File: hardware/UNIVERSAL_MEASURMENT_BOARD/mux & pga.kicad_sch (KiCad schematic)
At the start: 12 parts, among them Q1 NMOS, U1 PGA280AIPW, U2 CD4067BM96, U3 CD4067BM96

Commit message: continued
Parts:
- renumbered C8 to C10, C7 to C11, C9 to C12, C10 to C13, C6 to C7, C12 to C8, C11 to C9, U2 to U3, U1 to U4, U3 to U5
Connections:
- net +15V renamed +15VA
- net +3.3V renamed +3.3VA
- net -15V renamed -15VA
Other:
- company: (none) -> PUT Motorsport Formula Student team
- title: (none) -> Universal Measurment Board
- moved on the sheet: C10, C11, C12, C13, C7, C8, C9, Q1, R1, U3, U4, U5

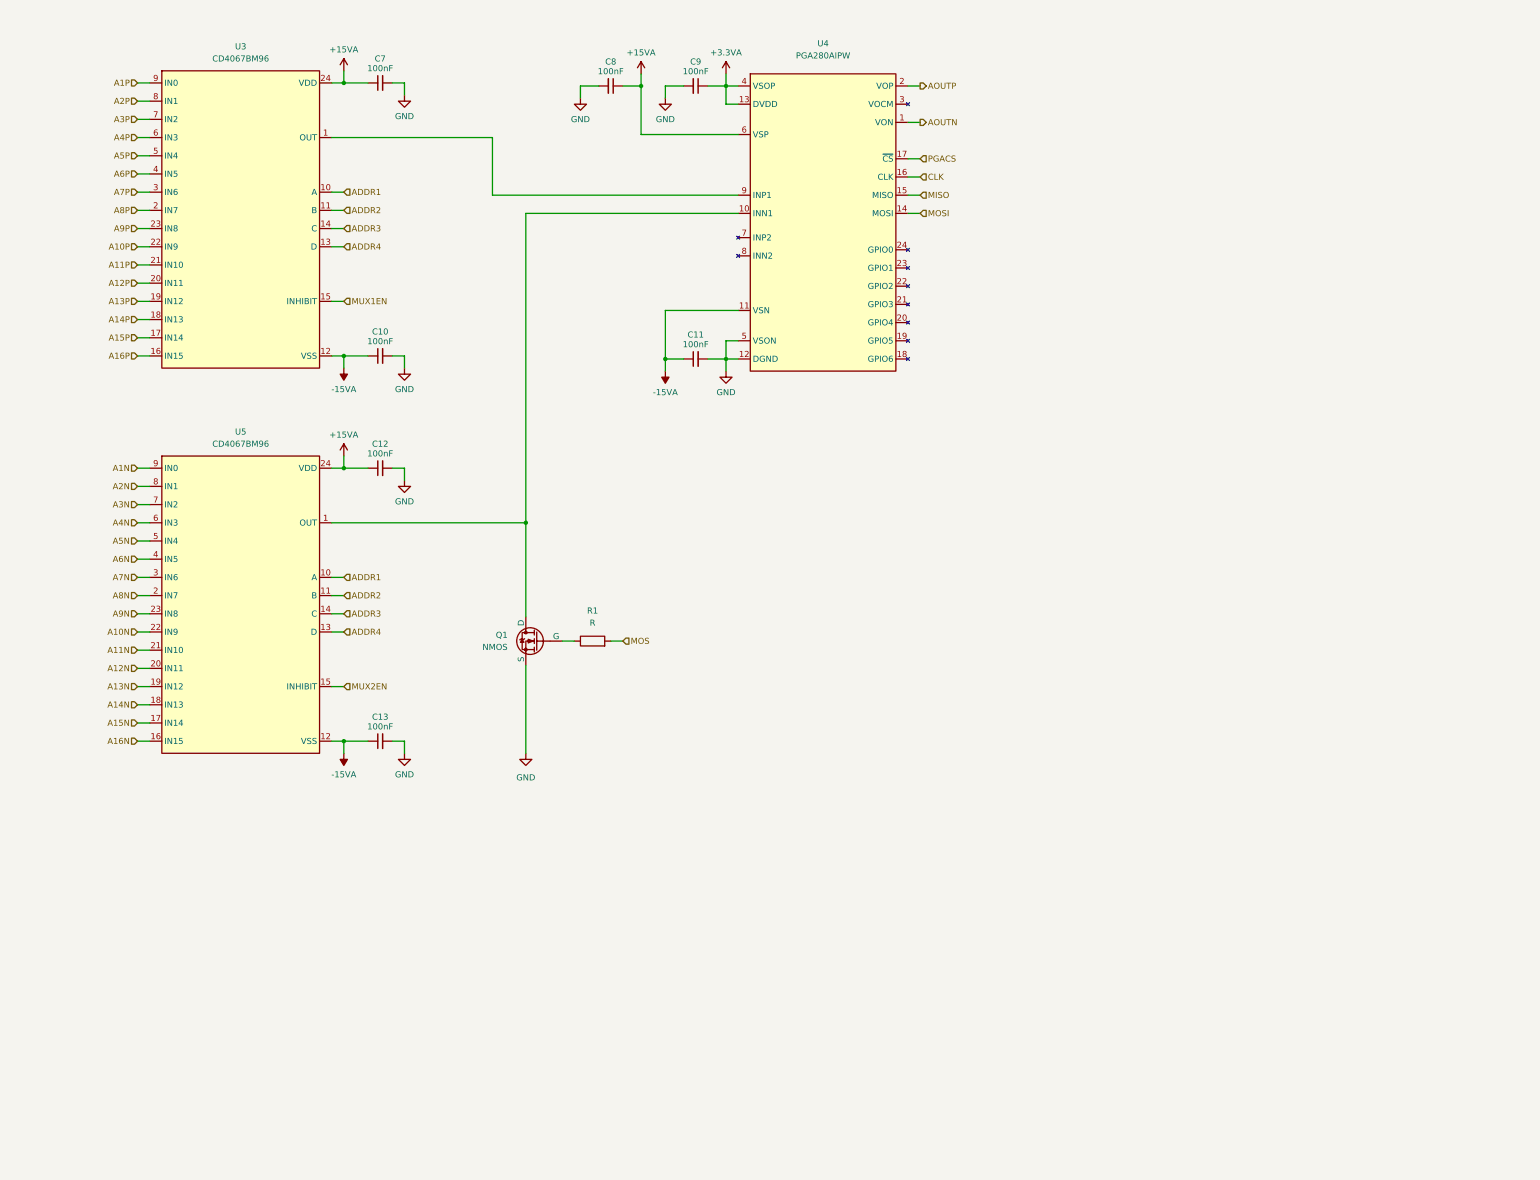
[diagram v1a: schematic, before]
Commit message: schematic review corrections
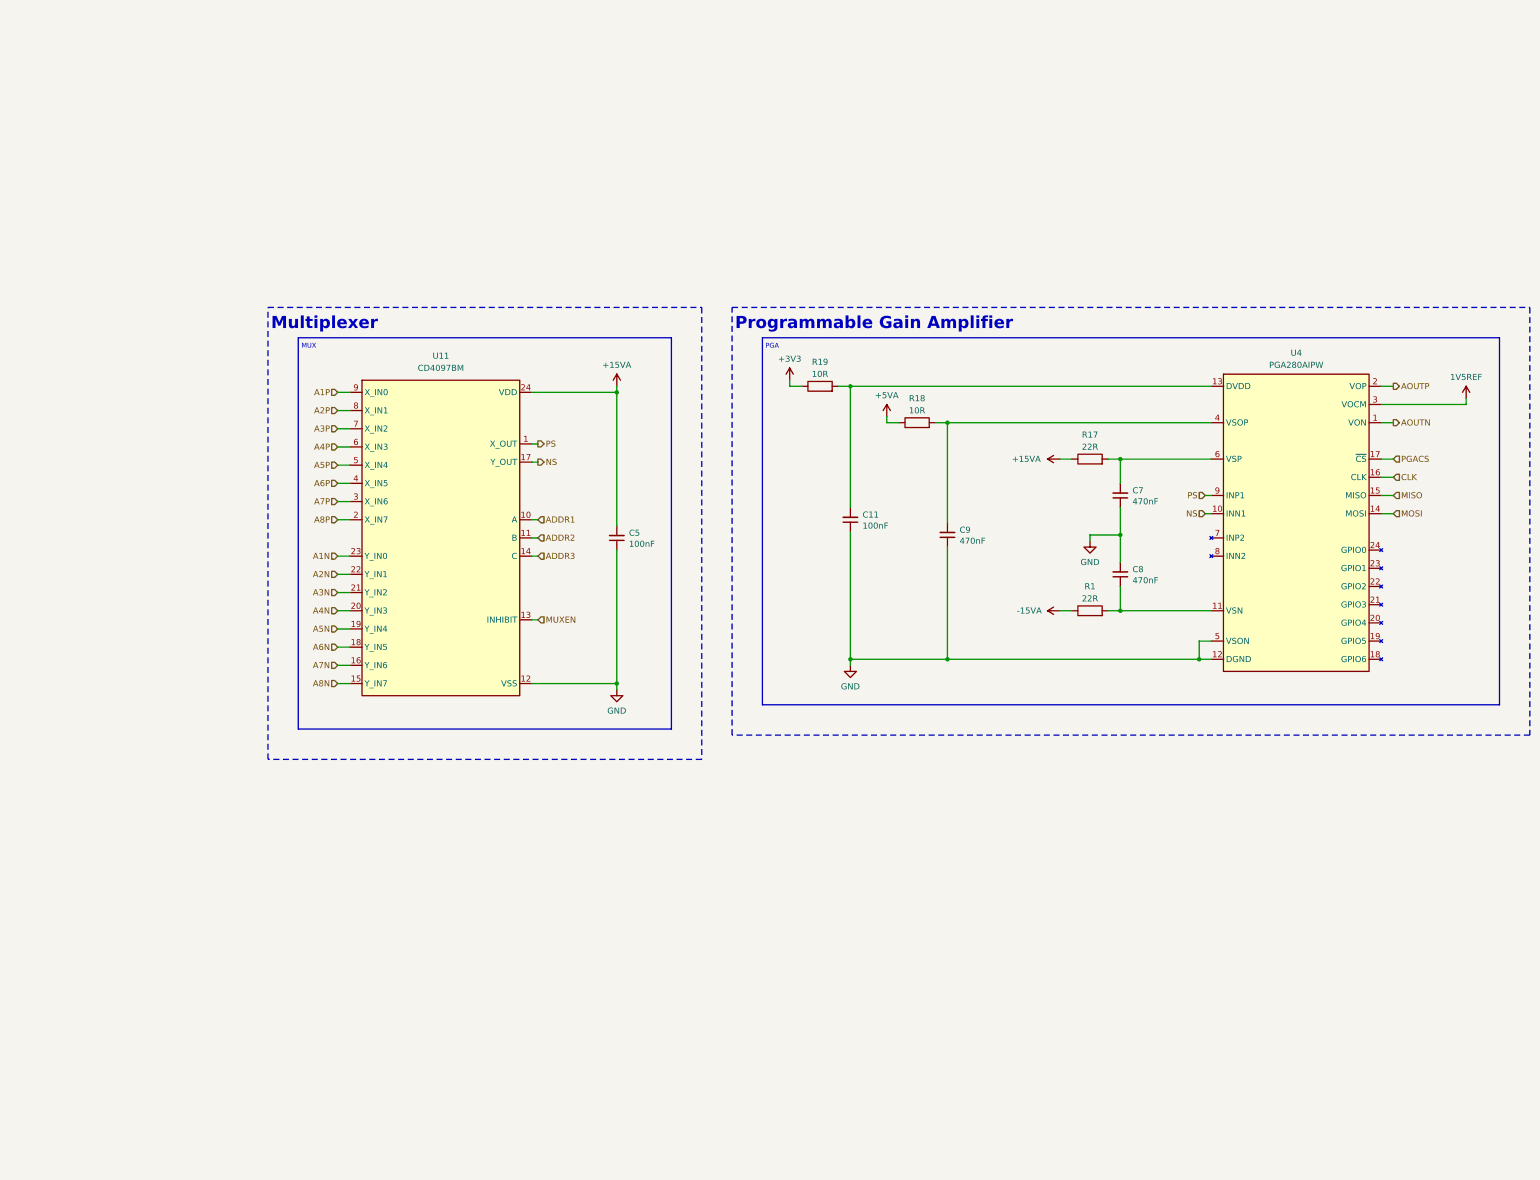
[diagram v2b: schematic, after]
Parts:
- removed C10, C12, C13: 100nF, symbol Device:C_Small
- removed Q1: NMOS, symbol Simulation_SPICE:NMOS
- removed U3, U5: CD4067BM96, SOIC127P1030X265-24N, symbol CD4067BM96:CD4067BM96
- added C5: 100nF, Capacitor_SMD:C_0805_2012Metric, symbol Device:C_Small
- added R17: 22R, symbol Device:R
- added R18, R19: 10R, symbol Device:R
- added U11: CD4097BM, SOIC127P1030X265-24N, symbol CD4097BM:CD4097BM
- C11: footprint (none) -> Capacitor_SMD:C_0805_2012Metric; Manufacturer_Name (none) -> MCASH21GCC7684MTCA1J; Manufacturer_Part_Number (none) -> CL21A107MQYNNWE; Mouser Part Number (none) -> 810-C2012X5R1V226MAC
- C7, C8, C9: value 100nF -> 470nF; footprint (none) -> Capacitor_SMD:C_0805_2012Metric; Manufacturer_Name (none) -> MCASH21GCC7684MTCA1J; Manufacturer_Part_Number (none) -> CL21A107MQYNNWE; Mouser Part Number (none) -> 810-C2012X5R1V226MAC
- R1: value R -> 22R
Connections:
- net +15VA: now also C5.2, R17.1, U11.24 (VDD); no longer C7.1, C8.1, U4.6 (VSP)
- net -15VA: now also R1.1; no longer C11.1, U4.11 (VSN)
- net A1N: now also U11.23 (Y_IN0)
- net A1P: now also U11.9 (X_IN0)
- net A2N: now also U11.22 (Y_IN1)
- net A2P: now also U11.8 (X_IN1)
- net A3N: now also U11.21 (Y_IN2)
- net A3P: now also U11.7 (X_IN2)
- net A4N: now also U11.20 (Y_IN3)
- net A4P: now also U11.6 (X_IN3)
- net A5N: now also U11.19 (Y_IN4)
- net A5P: now also U11.5 (X_IN4)
- net A6N: now also U11.18 (Y_IN5)
- net A6P: now also U11.4 (X_IN5)
- net A7N: now also U11.16 (Y_IN6)
- net A7P: now also U11.3 (X_IN6)
- net A8N: now also U11.15 (Y_IN7)
- net A8P: now also U11.2 (X_IN7)
- net ADDR1: now also U11.10 (A)
- net ADDR2: now also U11.11 (B)
- net ADDR3: now also U11.14 (C)
- net GND: now also C11.1, C7.1, C9.1, C5.1, U11.12 (VSS); no longer C11.2, C7.2, C9.2
- net NS: now reaches U4.10 (INN1)
- net NS: now also U11.17 (Y_OUT)
- net PS: now reaches U4.9 (INP1)
- net PS: now also U11.1 (X_OUT)
- net 1V5REF: now reaches U4.3 (VOCM)
- removed net +3.3VA: C9.1, U4.13 (DVDD), U4.4 (VSOP)
- net MOS: no longer names the net of R1.2
- net MOS: now also C8.1, U4.11 (VSN)
- new net: C7.2, R17.2, U4.6 (VSP)
- new net: C9.2, R18.2, U4.4 (VSOP)
- new net: C11.2, R19.2, U4.13 (DVDD)
- new net +3V3: R19.1
- new net +5VA: R18.1
- new net MUXEN: U11.13 (INHIBIT)
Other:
- note added: "MUX"
- note added: "Multiplexer"
- note added: "PGA"
- note added: "Programmable Gain Amplifier"

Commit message: final schematic review corrections
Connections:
- net +15VA renamed +15V0A
- net +5VA renamed +5V0A
- net -15VA renamed -15V0A
- net 1V5REF renamed 1V5A
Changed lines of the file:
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@@
 		(title "Universal Measurment Board")
 		(date "2026-02-02")
-		(rev "1.6.9")
+		(rev "1.7.14")
 		(company "PUT Motorsport Formula Student team")
 		(comment 1 "Designed by Marcin Trzmiel under")
@@
 	)
 	(junction
-		(at 217.805 157.48)
-		(diameter 0)
-		(color 0 0 0 0)
-	)
-	(junction
-		(at 197.485 157.48)
-		(diameter 0)
-		(color 0 0 0 0)
-	)
-	(junction
 		(at 270.51 157.48)
 		(diameter 0)
@@
 	)
 	(junction
-		(at 148.59 162.56)
-		(diameter 0)
-		(color 0 0 0 0)
-	)
-	(junction
 		(at 254 147.32)
 		(diameter 0)
@@
 	(wire
 		(pts
+			(xy 133.35 163.83) (xy 133.35 162.56)
+		)
+		(stroke
+			(width 0)
+			(type default)
+		)
+	)
+	(wire
+		(pts
 			(xy 184.785 99.06) (xy 184.785 100.33)
 		)
@@
 	(wire
 		(pts
+			(xy 270.51 158.75) (xy 270.51 157.48)
+		)
+		(stroke
+			(width 0)
+			(type default)
+		)
+	)
+	(wire
+		(pts
 			(xy 251.46 115.57) (xy 254 115.57)
 		)
@@
 	(wire
 		(pts
-			(xy 148.59 134.62) (xy 148.59 162.56)
-		)
-		(stroke
-			(width 0)
-			(type default)
-		)
-	)
-	(wire
-		(pts
 			(xy 273.05 100.33) (xy 197.485 100.33)
 		)
@@
 	(wire
 		(pts
-			(xy 197.485 130.81) (xy 197.485 157.48)
-		)
-		(stroke
-			(width 0)
-			(type default)
-		)
-	)
-	(wire
-		(pts
-			(xy 217.805 157.48) (xy 270.51 157.48)
+			(xy 197.485 130.81) (xy 197.485 158.75)
 		)
 		(stroke
@@
 	(wire
 		(pts
-			(xy 148.59 163.83) (xy 148.59 162.56)
-		)
-		(stroke
-			(width 0)
-			(type default)
-		)
-	)
-	(wire
-		(pts
-			(xy 197.485 158.75) (xy 197.485 157.48)
+			(xy 133.35 162.56) (xy 130.81 162.56)
+		)
+		(stroke
+			(width 0)
+			(type default)
+		)
+	)
+	(wire
+		(pts
+			(xy 148.59 134.62) (xy 148.59 163.83)
 		)
 		(stroke
@@
 	(wire
 		(pts
-			(xy 197.485 157.48) (xy 217.805 157.48)
-		)
-		(stroke
-			(width 0)
-			(type default)
-		)
-	)
-	(wire
-		(pts
 			(xy 132.08 112.395) (xy 130.81 112.395)
 		)
@@
 	(wire
 		(pts
-			(xy 130.81 162.56) (xy 148.59 162.56)
-		)
-		(stroke
-			(width 0)
-			(type default)
-		)
-	)
-	(wire
-		(pts
 			(xy 90.17 109.22) (xy 92.71 109.22)
 		)
@@
 	(wire
 		(pts
-			(xy 217.805 133.985) (xy 217.805 157.48)
+			(xy 217.805 133.985) (xy 217.805 158.75)
 		)
 		(stroke
@@
 			)
 		)
-		(property "Value" "+15VA"
+		(property "Value" "+15V0A"
 			(at 234.315 115.57 90)
 			(effects
@@
 	(symbol
 		(lib_id "power:GND")
+		(at 217.805 158.75 0)
+		(unit 1)
+		(exclude_from_sim no)
+		(in_bom yes)
+		(on_board yes)
+		(dnp no)
+		(property "Reference" "#PWR037"
+			(at 217.805 165.1 0)
+			(effects
+				(font
+					(size 1.27 1.27)
+				)
+				(hide yes)
+			)
+		)
+		(property "Value" "GND"
+			(at 217.805 163.195 0)
+			(effects
+				(font
+					(size 1.27 1.27)
+				)
+			)
+		)
+		(property "Footprint" ""
+			(at 217.805 158.75 0)
+			(effects
+				(font
+					(size 1.27 1.27)
+				)
+				(hide yes)
+			)
+		)
+		(property "Datasheet" ""
+			(at 217.805 158.75 0)
+			(effects
+				(font
+					(size 1.27 1.27)
+				)
+				(hide yes)
+			)
+		)
+		(property "Description" "Power symbol creates a global label with name \"GND\" , ground"
+			(at 217.805 158.75 0)
+			(effects
+				(font
+					(size 1.27 1.27)
+				)
+				(hide yes)
+			)
+		)
+		(pin "1"
+		)
+		(instances
+			(project "UNIVERSAL_MEASURMENT_BOARD"
+				(path "/92c00310-4384-4ef3-9368-efad75526047/2f9d6be2-539e-4cd2-829d-3839cc14b053"
+					(reference "#PWR037")
+					(unit 1)
+				)
+			)
+		)
+	)
+	(symbol
+		(lib_id "power:GND")
 		(at 148.59 163.83 0)
 		(mirror y)
@@
 			)
 		)
-		(property "Value" "+15VA"
+		(property "Value" "+15V0A"
 			(at 148.59 95.885 0)
 			(effects
@@
 			)
 		)
-		(property "Value" "1V5REF"
+		(property "Value" "1V5A"
 			(at 326.39 98.425 0)
 			(effects
@@
 			)
 		)
-		(property "Value" "-15VA"
+		(property "Value" "-15V0A"
 			(at 234.95 147.32 90)
 			(effects
@@
 				(path "/92c00310-4384-4ef3-9368-efad75526047/2f9d6be2-539e-4cd2-829d-3839cc14b053"
 					(reference "#PWR019")
+					(unit 1)
+				)
+			)
+		)
+	)
+	(symbol
+		(lib_id "power:GND")
+		(at 133.35 163.83 0)
+		(mirror y)
+		(unit 1)
+		(exclude_from_sim no)
+		(in_bom yes)
+		(on_board yes)
+		(dnp no)
+		(property "Reference" "#PWR043"
+			(at 133.35 170.18 0)
+			(effects
+				(font
+					(size 1.27 1.27)
+				)
+				(hide yes)
+			)
+		)
+		(property "Value" "GND"
+			(at 133.35 168.275 0)
+			(effects
+				(font
+					(size 1.27 1.27)
+				)
+			)
+		)
+		(property "Footprint" ""
+			(at 133.35 163.83 0)
+			(effects
+				(font
+					(size 1.27 1.27)
+				)
+				(hide yes)
+			)
+		)
+		(property "Datasheet" ""
+			(at 133.35 163.83 0)
+			(effects
+				(font
+					(size 1.27 1.27)
+				)
+				(hide yes)
+			)
+		)
+		(property "Description" "Power symbol creates a global label with name \"GND\" , ground"
+			(at 133.35 163.83 0)
+			(effects
+				(font
+					(size 1.27 1.27)
+				)
+				(hide yes)
+			)
+		)
+		(pin "1"
+		)
+		(instances
+			(project "UNIVERSAL_MEASURMENT_BOARD"
+				(path "/92c00310-4384-4ef3-9368-efad75526047/2f9d6be2-539e-4cd2-829d-3839cc14b053"
+					(reference "#PWR043")
 					(unit 1)
 				)
@@
 	)
 	(symbol
+		(lib_id "power:GND")
+		(at 270.51 158.75 0)
+		(unit 1)
+		(exclude_from_sim no)
+		(in_bom yes)
+		(on_board yes)
+		(dnp no)
+		(property "Reference" "#PWR038"
+			(at 270.51 165.1 0)
+			(effects
+				(font
+					(size 1.27 1.27)
+				)
+				(hide yes)
+			)
+		)
+		(property "Value" "GND"
+			(at 270.51 163.195 0)
+			(effects
+				(font
+					(size 1.27 1.27)
+				)
+			)
+		)
+		(property "Footprint" ""
+			(at 270.51 158.75 0)
+			(effects
+				(font
+					(size 1.27 1.27)
+				)
+				(hide yes)
+			)
+		)
+		(property "Datasheet" ""
+			(at 270.51 158.75 0)
+			(effects
+				(font
+					(size 1.27 1.27)
+				)
+				(hide yes)
+			)
+		)
+		(property "Description" "Power symbol creates a global label with name \"GND\" , ground"
+			(at 270.51 158.75 0)
+			(effects
+				(font
+					(size 1.27 1.27)
+				)
+				(hide yes)
+			)
+		)
+		(pin "1"
+		)
+		(instances
+			(project "UNIVERSAL_MEASURMENT_BOARD"
+				(path "/92c00310-4384-4ef3-9368-efad75526047/2f9d6be2-539e-4cd2-829d-3839cc14b053"
+					(reference "#PWR038")
+					(unit 1)
+				)
+			)
+		)
+	)
+	(symbol
 		(lib_id "Device:R")
 		(at 247.65 147.32 90)
@@
 			)
 		)
-		(property "Value" "+5VA"
+		(property "Value" "+5V0A"
 			(at 205.105 102.235 0)
 			(effects
